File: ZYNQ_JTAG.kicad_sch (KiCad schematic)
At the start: 1 part, among them U1 XC7Z020-2CLG484I

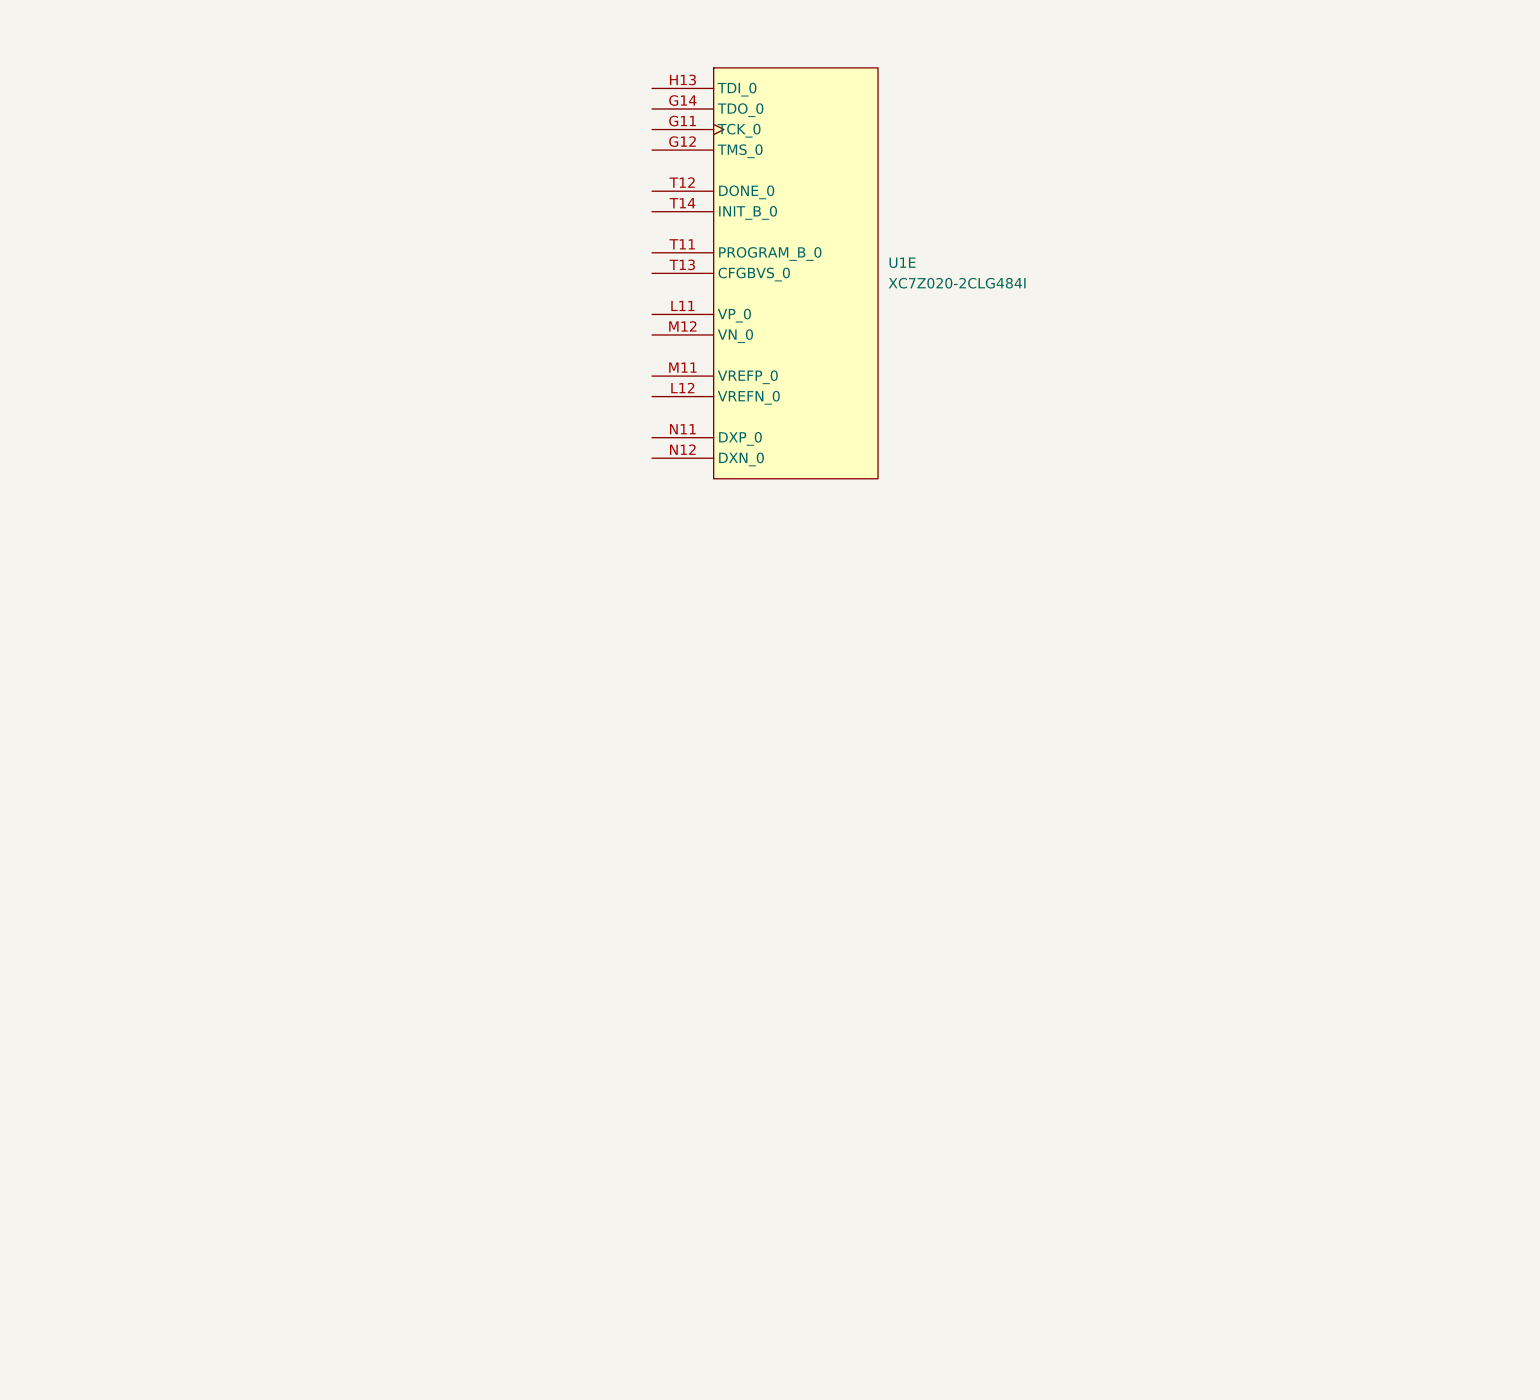
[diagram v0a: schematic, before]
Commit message: Update JTAG and SDR schematics and libraries
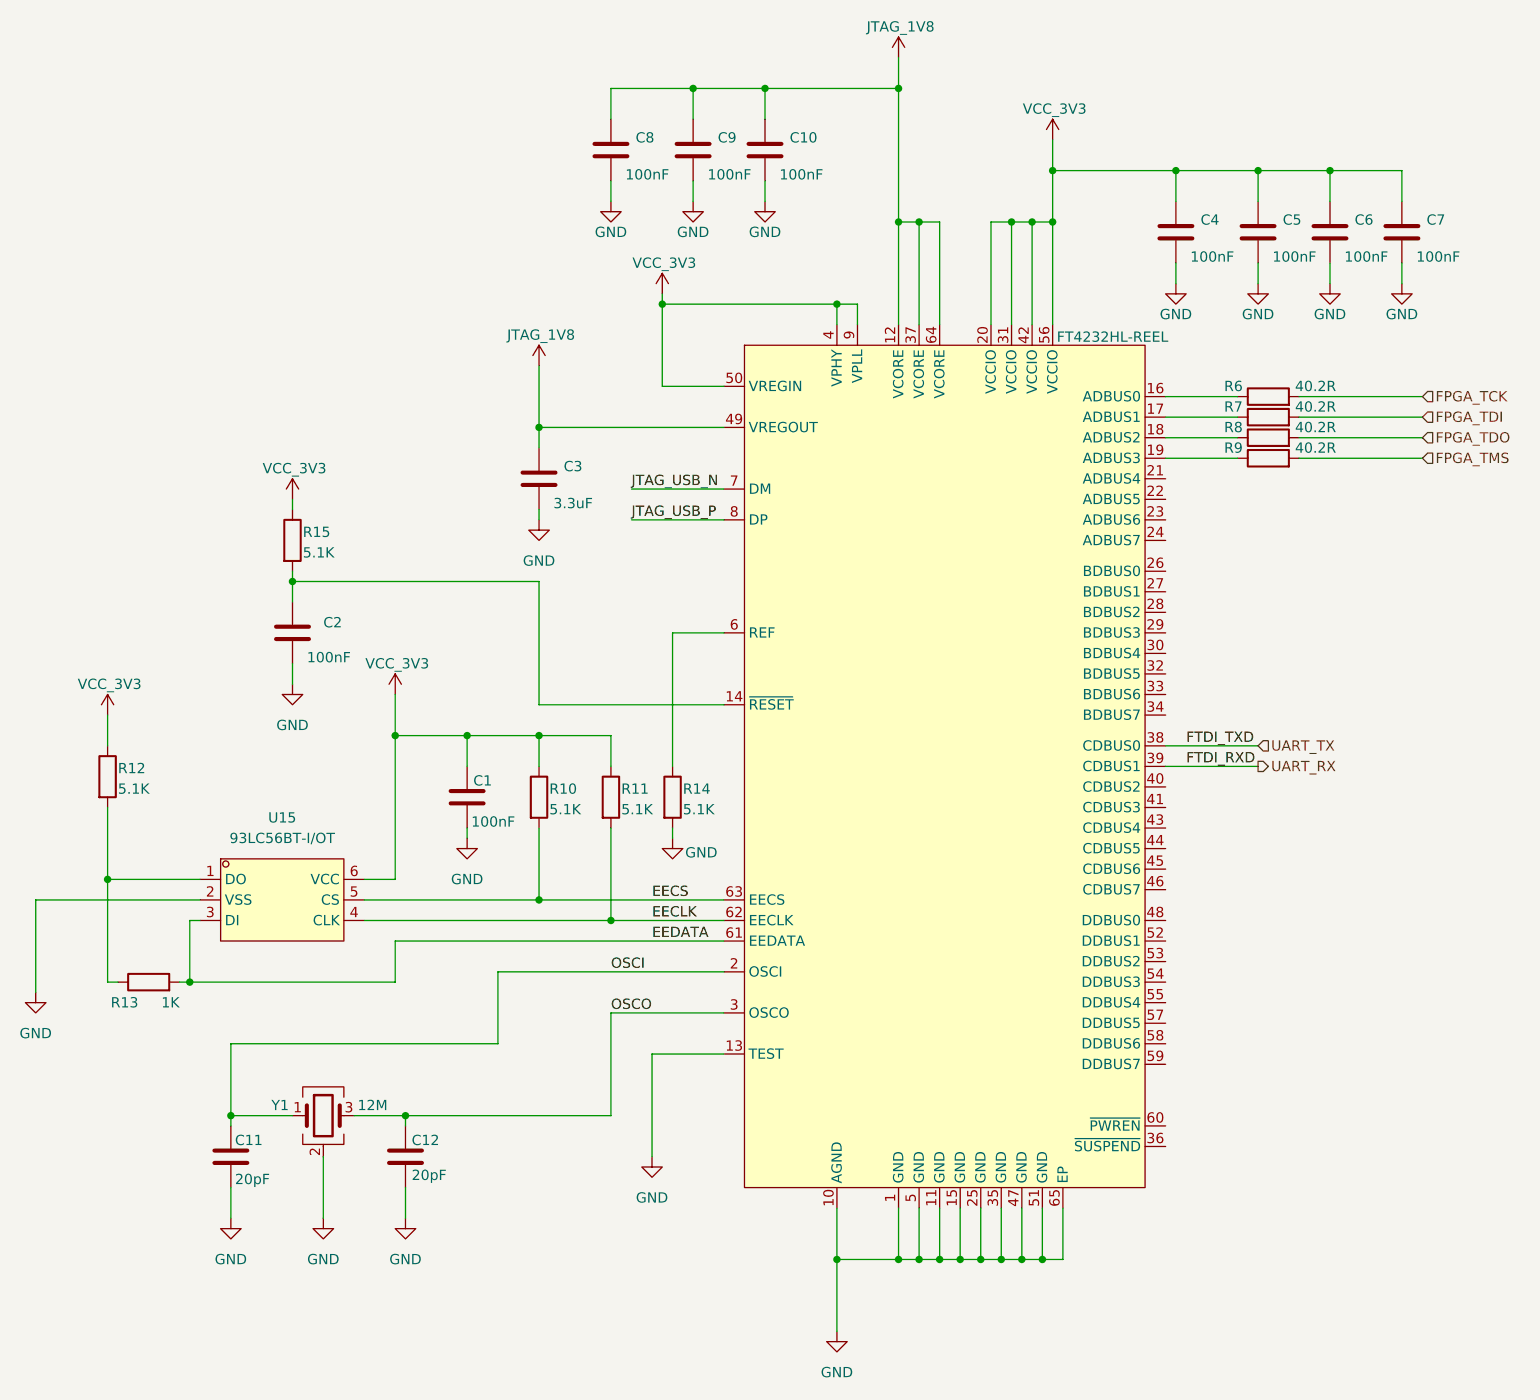
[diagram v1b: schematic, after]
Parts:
- removed U1: XC7Z020-2CLG484I, easyeda2kicad:FPBGA-484_L19.0-W19.0-R22-C22-P0.80-BL, symbol ZYNQ7020_SDR:XC7Z020-2CLG484I
- added C1, C10, C2, C4, C5, C6, C7, C8, C9: 100nF, symbol Device:C
- added C11, C12: 20pF, symbol Device:C
- added C3: 3.3uF, symbol Device:C
- added R10, R11, R12, R14, R15: 5.1K, symbol Device:R
- added R13: 1K, symbol Device:R
- added R6, R7, R8, R9: 40.2R, symbol Device:R
- added U15: 93LC56BT-I/OT, easyeda2kicad:SOT-23-6_L2.9-W1.6-P0.95-LS2.8-BR, symbol ZYNQ7020_SDR:93LC56BT-I_OT
- added U7: FT4232HL-REEL, easyeda2kicad:LQFP-64_L10.0-W10.0-P0.50-LS12.0-TL, symbol ZYNQ7020_SDR:FT4232HL-REEL
- added Y1: 12M, Crystal:Crystal_SMD_3225-4Pin_3.2x2.5mm_HandSoldering, symbol Device:Crystal_GND24
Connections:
- new net: C2.1, R15.2, U7.14 (~{RESET})
- new net: R6.1, U7.16 (ADBUS0)
- new net: R7.1, U7.17 (ADBUS1)
- new net: R8.1, U7.18 (ADBUS2)
- new net: R9.1, U7.19 (ADBUS3)
- new net: R14.1, U7.6 (REF)
- new net: R12.2, R13.1, U15.1 (DO)
- new net EECLK: R11.2, U15.4 (CLK), U7.62 (EECLK)
- new net EECS: R10.2, U15.5 (CS), U7.63 (EECS)
- new net EEDATA: R13.2, U15.3 (DI), U7.61 (EEDATA)
- new net FPGA_TCK: R6.2
- new net FPGA_TDI: R7.2
- new net FPGA_TDO: R8.2
- new net FPGA_TMS: R9.2
- new net GND: C1.2, C10.2, C11.2, C12.2, C2.2, C3.2, C4.2, C5.2, C6.2, C7.2, C8.2, C9.2, R14.2, U15.2 (VSS), U7.1 (GND), U7.10 (AGND), U7.11 (GND), U7.13 (TEST), U7.15 (GND), U7.25 (GND), U7.35 (GND), U7.47 (GND), U7.5 (GND), U7.51 (GND), U7.65 (EP), Y1.2 (G), Y1.4 (G)
- new net JTAG_1V8: C10.1, C3.1, C8.1, C9.1, U7.12 (VCORE), U7.37 (VCORE), U7.49 (VREGOUT), U7.64 (VCORE)
- new net JTAG_USB_N: U7.7 (DM)
- new net JTAG_USB_P: U7.8 (DP)
- new net OSCI: C11.1, U7.2 (OSCI), Y1.1
- new net OSCO: C12.1, U7.3 (OSCO), Y1.3
- new net UART_RX: U7.39 (CDBUS1)
- new net UART_TX: U7.38 (CDBUS0)
- new net VCC_3V3: C1.1, C4.1, C5.1, C6.1, C7.1, R10.1, R11.1, R12.1, R15.1, U15.6 (VCC), U7.20 (VCCIO), U7.31 (VCCIO), U7.4 (VPHY), U7.42 (VCCIO), U7.50 (VREGIN), U7.56 (VCCIO), U7.9 (VPLL)
